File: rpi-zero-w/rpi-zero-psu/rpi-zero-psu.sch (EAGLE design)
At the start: 21 parts, among them J1 M20X2, J2 POWER_JACKPTH, Q1 DMG2305UX, Q2 DMG2302UK-7, U2 MP2307-MODULE, U4 DMMT5401

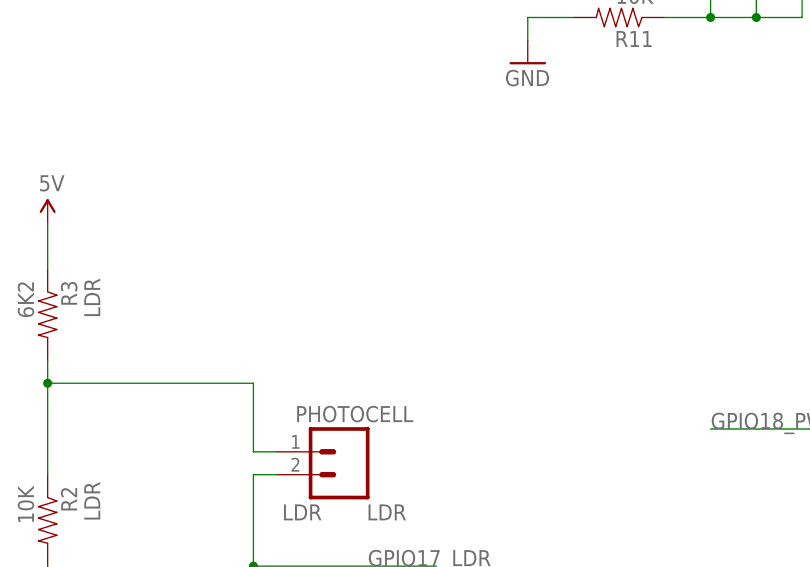
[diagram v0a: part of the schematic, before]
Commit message: rpi-zero-psu: removed milling layer
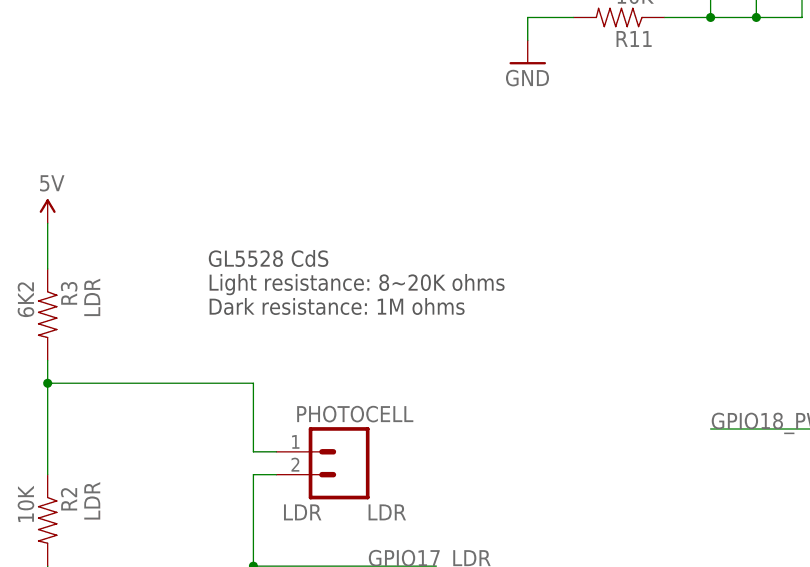
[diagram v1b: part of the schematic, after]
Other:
- note added: "GL5528 CdS Light resistance: 8~20K ohms Dark resistance: 1M ohms"
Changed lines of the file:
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@@
 <wire x1="124.46" y1="111.76" x2="60.96" y2="111.76" width="0.1524" layer="97" style="shortdash"/>
 <wire x1="60.96" y1="111.76" x2="60.96" y2="152.4" width="0.1524" layer="97" style="shortdash"/>
+<text x="114.3" y="71.12" size="1.778" layer="97">GL5528 CdS
+Light resistance: 8~20K ohms
+Dark resistance: 1M ohms</text>
 </plain>
 <instances>
